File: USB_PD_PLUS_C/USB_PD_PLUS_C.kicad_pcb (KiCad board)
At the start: 4 copper layers, 60 x 60 mm, 128 parts, among them J1 USB3_A, J2 USB3_A, J3 USB3_A, Q2 FS8205A_C908265, Q3 FS8205A_C908265, Q4 FS8205A_C908265, U1 NDP1360KC, U10 NDP1360KC, U11 CXP0650-220M-AG(22UH), U12 TPS25740ARGER, U13 NDP1360KC, U14 CXP0650-220M-AG(22UH), U15 TPS25740ARGER, U16 NDP1360KC, U17 CXP0650-220M-AG(22UH), U18 TPS25740ARGER, U3 CH482D, U4 CXP0650-220M-AG(22UH), U5 LM317L_SOT-89, U6 CH482D, U7 CH482D

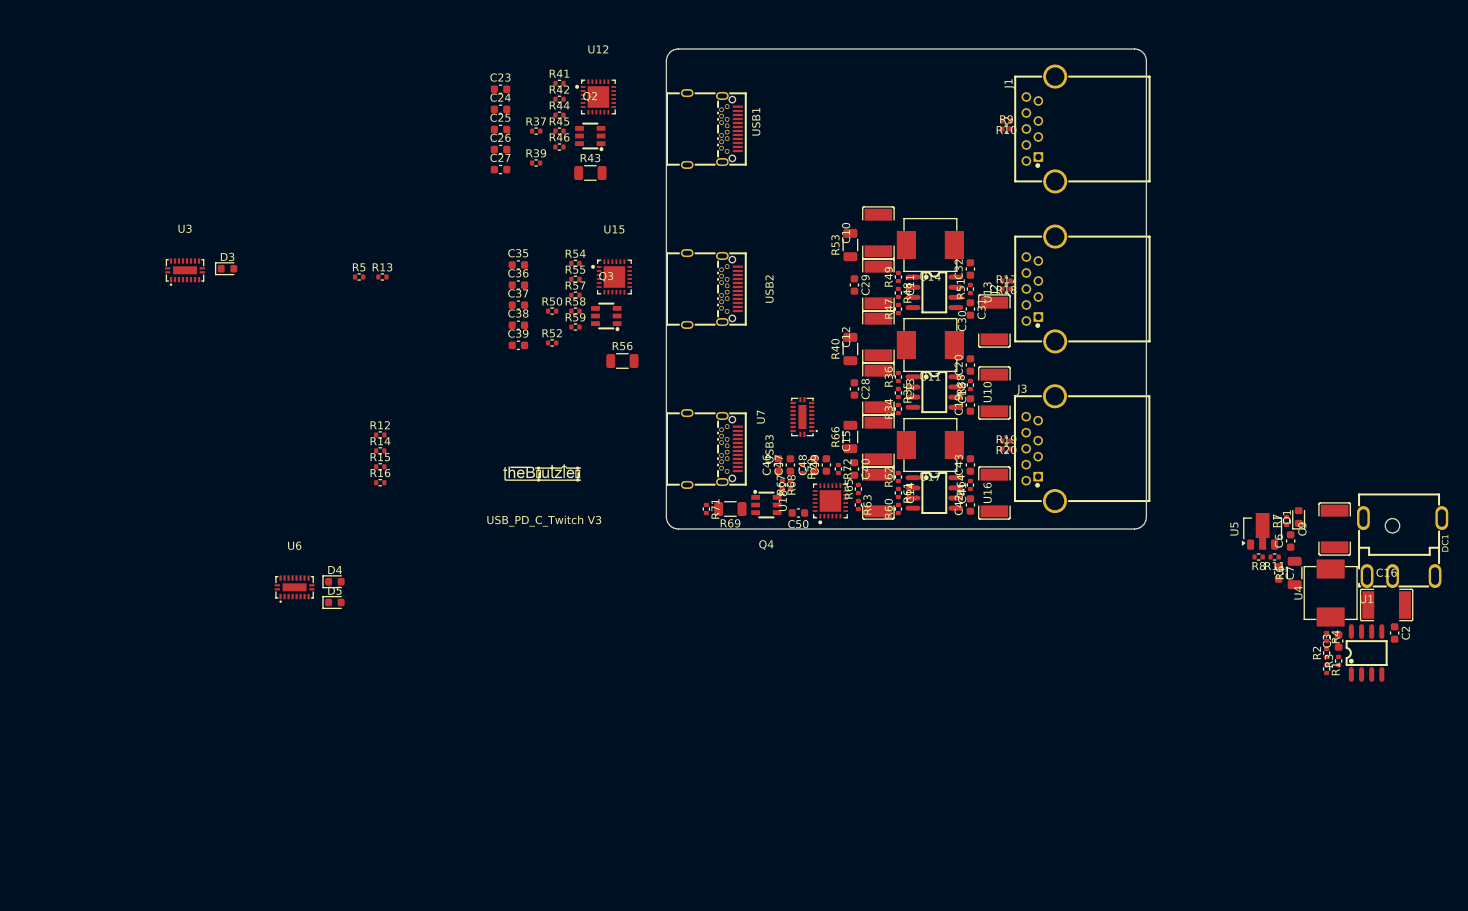
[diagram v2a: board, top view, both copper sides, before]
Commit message: update routing usb c pd
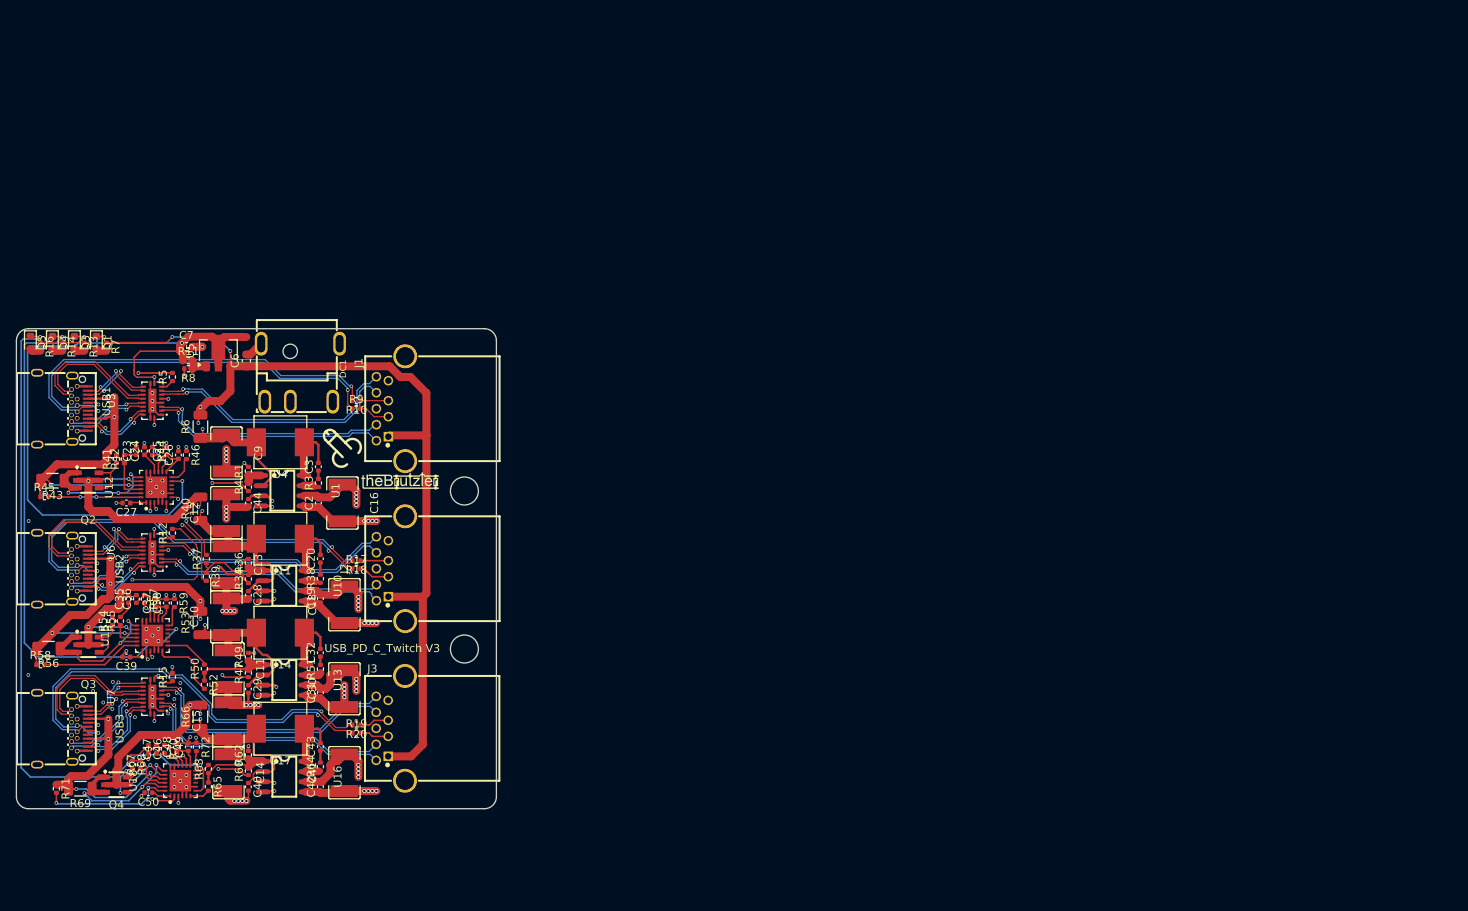
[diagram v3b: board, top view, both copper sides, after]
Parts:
- removed R2, R35, R48, R61: 8K, Resistor_SMD:R_0402_1005Metric
- added C44: 100n, Capacitor_SMD:C_0402_1005Metric, F.Cu at (126.8, 81.8)
- added REF**: penoid, theBrutzler:penoid, F.Cu at (138.0, 74.5)
- C19, C2, C20, C23, C24, C25, C26, C27, C28, C29, C3, C31, C32, C35, C36, C37, C38, C39, C40, C42, C43, C46, C47, C48, C49, C50: footprint Capacitor_SMD:C_0603_1608Metric -> Capacitor_SMD:C_0402_1005Metric
- R34, R4, R47, R60: value 100K -> 107K
- moved D1 151.9 mm to (107.8, 61.7), turned to -90 degrees
- moved R7 149.1 mm to (109.0, 62.2), turned to -90 degrees
- moved DC1 139.5 mm to (133.2, 65.5)
- moved C7 139.4 mm to (119.0, 62.2), turned to 0 degrees
- moved C9 138.9 mm to (124.0, 75.5), turned to -90 degrees
- moved R6 138.0 mm to (120.8, 72.2)
- moved R11 138.0 mm to (119.2, 64.0), turned to 0 degrees
- moved U1 137.0 mm to (131.0, 80.2), turned to -90 degrees
- moved R1 137.0 mm to (126.8, 77.8), turned to 90 degrees
- moved R4 136.1 mm to (126.8, 79.8), turned to 90 degrees
- moved R8 135.8 mm to (119.2, 65.0)
- moved C2 135.5 mm to (135.5, 81.8), turned to 90 degrees
- moved U4 132.6 mm to (130.8, 74.2), turned to 180 degrees
- moved C6 132.5 mm to (126.5, 64.0)
- moved U5 132.4 mm to (123.0, 62.7)
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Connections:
- R34 pad 2: Net-(R34-Pad2) -> Net-(U10-FB)
- R4 pad 2: Net-(R2-Pad2) -> Net-(U1-FB)
- R47 pad 2: Net-(R47-Pad2) -> Net-(U13-FB)
- R60 pad 2: Net-(R60-Pad2) -> Net-(U16-FB)
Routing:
- net +3V3: track 0.00 -> 160.5 mm, vias 0 -> 13
- net GND: track 0.00 -> 153.5 mm, vias 0 -> 90
- net +5V: track 0.00 -> 146.7 mm, vias 0 -> 6
- net +24V: track 0.00 -> 96.9 mm, vias 0 -> 16
- net /USB_PD3/USB1_CC_~{DET}: track 0.00 -> 83.5 mm, vias 0 -> 2
- net /USB_PD2/USB1_CC_~{DET}: track 0.00 -> 66.0 mm, vias 0 -> 2
- net Net-(U10-CSN2): track 0.00 -> 65.6 mm, vias 0 -> 6
- net Net-(U13-CSN2): track 0.00 -> 63.5 mm, vias 0 -> 6
- net Net-(U16-CSN2): track 0.00 -> 61.9 mm, vias 0 -> 6
- net /C_D-: track 0.00 -> 54.5 mm, vias 0 -> 2
- net /C_D+: track 0.00 -> 52.8 mm, vias 0 -> 1
- net /USB_PD1/USB1_CC_~{DET}: track 0.00 -> 52.7 mm, vias 0 -> 2
- net /A_D-: track 0.00 -> 52.5 mm, vias 0 -> 2
- net /B_D-: track 0.00 -> 51.4 mm, vias 0 -> 2
- net /A_D+: track 0.00 -> 50.6 mm, vias 0 -> 1
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- added copper zone on In1.Cu, net GND
- added copper zone on In2.Cu, net GND
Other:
- outline, holes or cut-outs redrawn

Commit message: CC Bug
there was a error, to detect cable orientation. now it should work
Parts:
- removed R12, R15, R5: 0R, Resistor_SMD:R_0402_1005Metric
- added U2: LM321, Package_TO_SOT_SMD:SOT-23-5, F.Cu at (114.8, 64.2)
- added U8: LM321, Package_TO_SOT_SMD:SOT-23-5, F.Cu at (104.2, 82.8)
- added U9: LM321, Package_TO_SOT_SMD:SOT-23-5, F.Cu at (103.8, 103.0)
- moved R58 0.71 mm to (100.8, 101.2)
- moved R56 0.46 mm to (101.8, 99.5)
- moved R45 0.21 mm to (101.2, 80.8)
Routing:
- net /A_CC1: track 29.9 -> 52.2 mm
- net /A_CC2: track 22.2 -> 41.9 mm
- net Net-(U7-SEL): track 1.42 -> 14.3 mm
- net Net-(U6-SEL): track 1.43 -> 13.4 mm
- net /B_CC2: track 21.3 -> 30.1 mm
- net /C_CC2: track 23.1 -> 31.9 mm
- net +3V3: track 160.5 -> 169.1 mm, vias 13 -> 14
- net /B_CC1: track 40.0 -> 44.6 mm
- net GND: track 153.5 -> 157.7 mm, vias 90 -> 93
- net /C_CC1: track 40.4 -> 44.1 mm
- net /B1_SSRX+: track 17.9 -> 15.1 mm
- net /B1_SSRX-: track 18.9 -> 16.3 mm
- net Net-(Q2-S1): track 19.4 -> 21.8 mm
- net +5V: track 146.7 -> 148.7 mm
- net Net-(U3-SEL): track 1.63 -> 3.27 mm
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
